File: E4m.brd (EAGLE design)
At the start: 50 x 100 mm, 78 parts, among them Q1 IRL540, Q2 IRL540, Q3 tip120

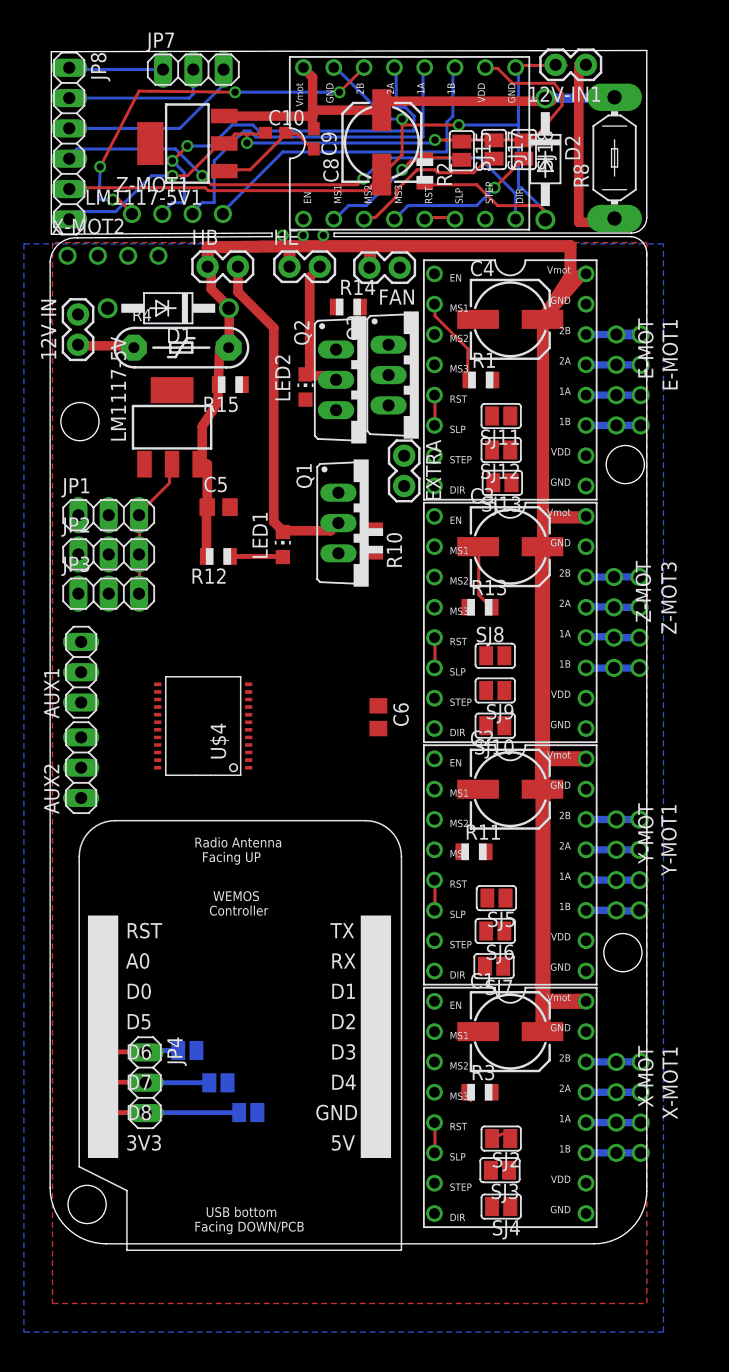
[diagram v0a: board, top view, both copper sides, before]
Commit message: Add files via upload
reposition several elements for better routing
routing done

todo 1: fix 2 holes used for mounting/fixing the board
todo 2: check all drc on file
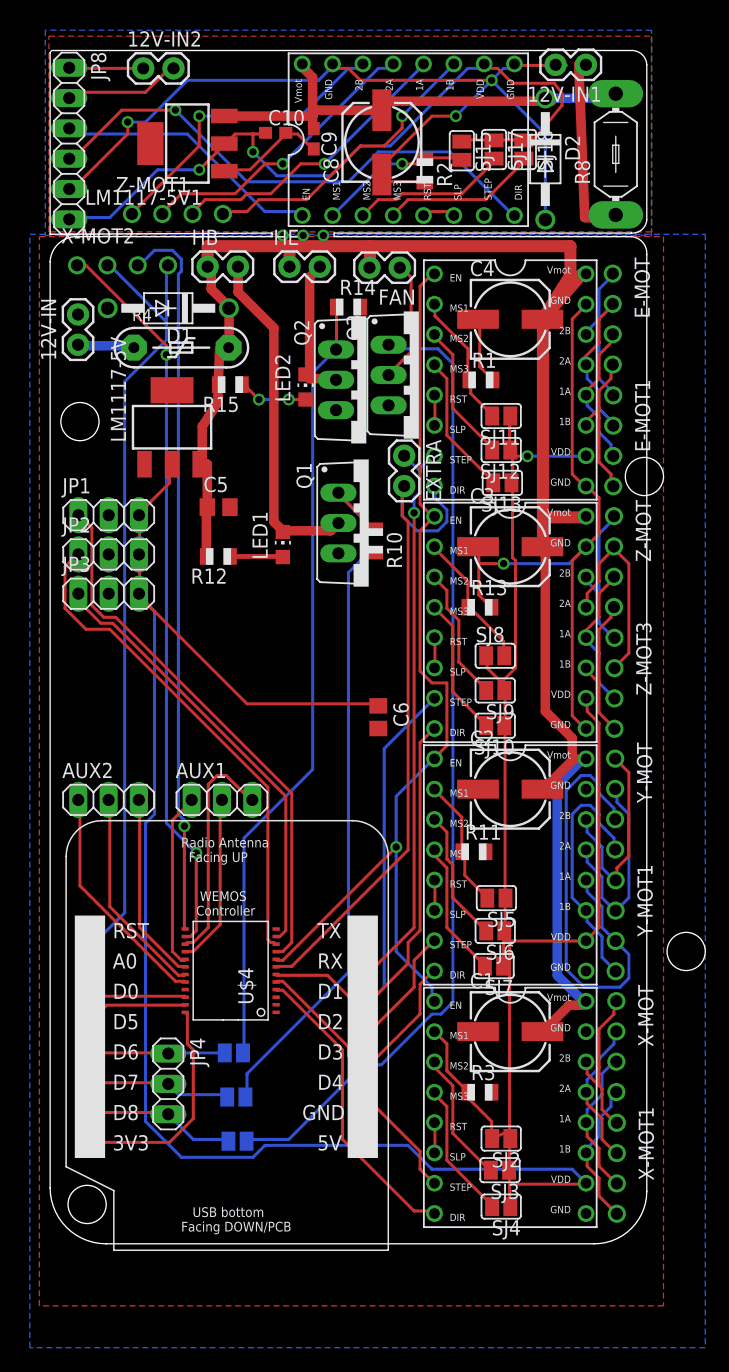
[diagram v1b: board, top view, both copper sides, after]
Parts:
- removed JP7: (no value), pinhead:1X03
- added 12V-IN2: (no value), SparkFun:1X02
- moved U$4 20.6 mm to (15.1, 22.9)
- moved AUX1 15.9 mm to (14.4, 37.2), turned to 0 degrees
- moved E-MOT1 5.59 mm to (47.2, 68.6)
- moved Z-MOT3 5.52 mm to (47.3, 48.2)
- moved Y-MOT1 5.48 mm to (47.4, 27.9)
- moved X-MOT1 5.48 mm to (47.5, 7.60)
- moved E-MOT 5.11 mm to (47.1, 78.8)
- moved Y-MOT 5.10 mm to (47.4, 38.1)
- moved X-MOT 5.10 mm to (47.5, 17.8)
- moved Z-MOT 5.10 mm to (47.2, 58.4)
- moved SJ14 3.91 mm to (15.4, 16.0)
- moved AUX2 3.55 mm to (4.90, 37.2), turned to 0 degrees
- moved SJ16 2.56 mm to (15.7, 8.60)
- moved SJ1 1.92 mm to (15.6, 12.3)
- moved JP4 1.90 mm to (9.90, 13.4)
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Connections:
- removed net N$51: JP7.3, JP8.3
- net ENABLE1: now also JP8.3
- net N$52: now also 12V-IN2.2; no longer JP7.2
- net N$53: now also 12V-IN2.1; no longer JP7.1
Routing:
- net 5V: track 12.1 -> 235.8 mm, vias 0 -> 1
- net N$27: track 0.00 -> 81.7 mm
- net ENABLE: track 0.00 -> 81.5 mm, vias 0 -> 1
- net ANALOG: track 0.00 -> 68.2 mm
- net N$23: track 0.00 -> 65.8 mm
- net S-A1: track 0.00 -> 61.5 mm, vias 0 -> 2
- net S-A0: track 0.00 -> 60.9 mm, vias 0 -> 1
- net N$S4: track 0.00 -> 59.9 mm
- net E-DIR: track 0.00 -> 56.7 mm
- net GND: track 6.19 -> 60.1 mm, vias 0 -> 1
- net E-STEP: track 0.00 -> 49.3 mm, vias 0 -> 1
- net X-STOP: track 0.00 -> 45.5 mm
- net Y-STOP: track 0.00 -> 41.8 mm
- net Z-STOP: track 0.00 -> 37.0 mm
- net Z-DIR: track 0.00 -> 34.2 mm
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- added copper zone on layer 1, net GND1
- added copper zone on layer 16, net GND1
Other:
- outline, holes or cut-outs redrawn
